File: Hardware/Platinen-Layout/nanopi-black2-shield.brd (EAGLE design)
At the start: 40 x 40 mm, 12 parts, among them IC2 LM3940IT-3.3

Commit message: new hardware + test code
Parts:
- added J3: (no value), 61300211821_Eagle_WR-PHD_rev19a:61300211121
- added R4, R5: 2.2k, SparkFun-Resistors:0603
- moved J5 0.42 mm to (38.4, 19.8), turned to 270 degrees
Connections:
- net 3.3V: now also R4.2, R5.2
- net 5V-1: now also J3.2
- net GND: now also J3.1
- net I2C_SCL0: now also R5.1
- net I2C_SDA0: now also R4.1
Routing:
- net 5V-1: track 31.1 -> 50.2 mm
- net 3.3V: track 15.3 -> 25.0 mm
- net GPIOA0: track 30.1 -> 24.4 mm
- net I2C_SCL0: track 34.9 -> 40.6 mm
- net I2C_SDA0: track 40.6 -> 36.4 mm
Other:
- outline, holes or cut-outs redrawn
- board text added: "5V_Ex"

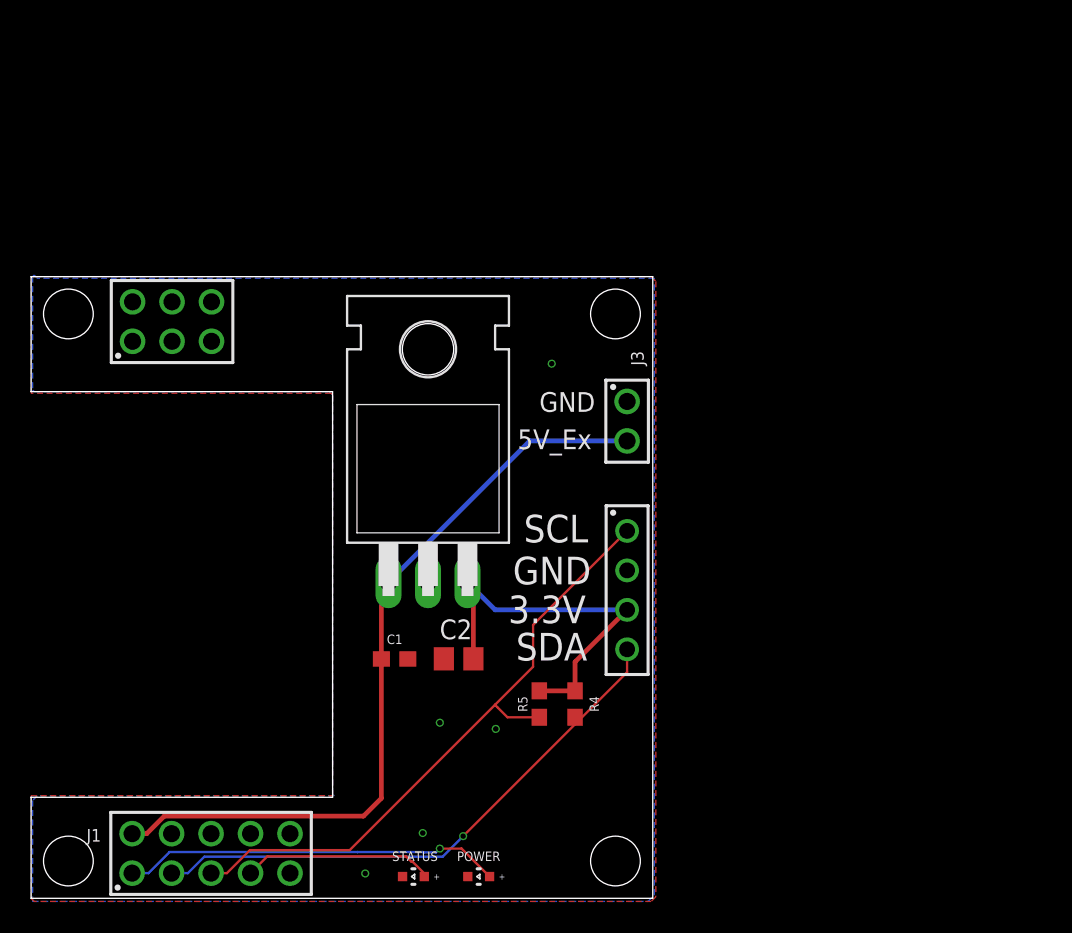
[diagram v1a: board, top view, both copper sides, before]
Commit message: new adapter Board
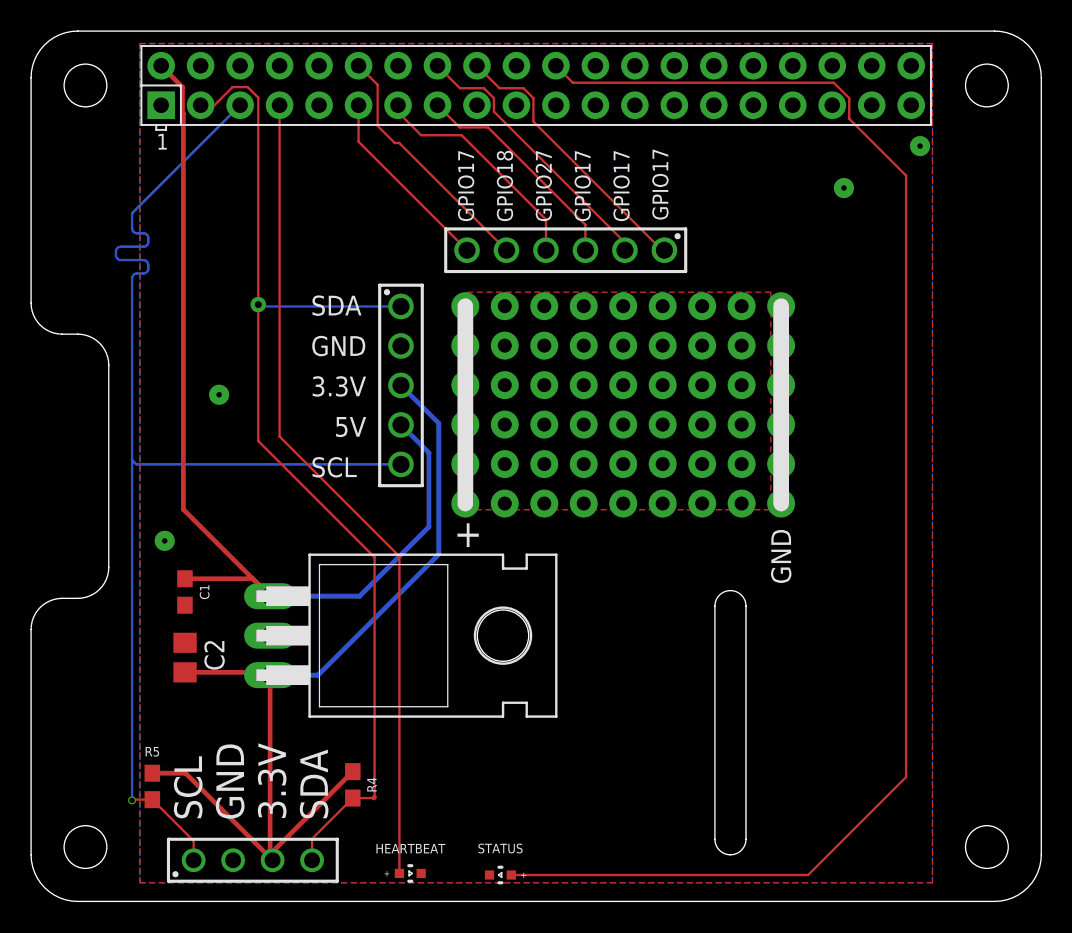
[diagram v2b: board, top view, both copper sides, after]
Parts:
- removed J3: (no value), 61300211821_Eagle_WR-PHD_rev19a:61300211121
- removed POWER: (no value), 155060GS75300_Eagle_WL-SMSW_rev20b:WL-SMSW_0603_REC
- removed U$1, U$2, U$3, U$4: (no value), M3-Hole:3-2MM-HOLE
- added HEARTBEAT: (no value), 155060GS75300_Eagle_WL-SMSW_rev20b:WL-SMSW_0603_REC
- added X1: RASPI_BOARD_B+#_HDC, raspberrypi_bastelstube_v13:RASPI_BOARD_B+HAT_DF_CF
- J1: device 61300211821_Eagle_WR-PHD_rev19a:61301021121 -> 61300621821_Eagle_WR-PHD_rev19a:61300511121
- J2: device 61300211821_Eagle_WR-PHD_rev19a:61300621121 -> 61300621821_Eagle_WR-PHD_rev19a:61300611121
- moved J1 32.5 mm to (23.8, 33.0), turned to 270 degrees
- moved J5 29.7 mm to (14.3, 2.45), turned to 0 degrees
- moved J2 25.7 mm to (34.4, 41.7), turned to 180 degrees
- moved R5 25.5 mm to (7.80, 7.20)
- moved C2 17.6 mm to (9.91, 15.5), turned to 90 degrees
- moved R4 15.2 mm to (20.7, 7.30)
- moved C1 14.2 mm to (9.90, 19.7), turned to 270 degrees
- moved IC2 13.6 mm to (25.5, 16.9), turned to 270 degrees
- moved STATUS 5.60 mm to (30.2, 1.50)
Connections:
- removed net 5V-2: J1.4
- removed net GPIOA0: J1.1, POWER.2
- removed net GPIOA2: J1.7, STATUS.2
- removed net UART1_RX: J1.10
- removed net UART1_TX: J1.8
- new net 3V3A: X1.1
- new net 3V3B: X1.17
- new net 5V0B: X1.4
- new net GND_A: X1.6
- new net GND_B: X1.9
- new net GND_C: X1.14
- new net GND_D: X1.20
- new net GND_E: X1.25
- new net GND_F: X1.30
- new net GND_G: X1.34
- new net GPIO04: HEARTBEAT.2, X1.7
- new net GPIO17: J2.6, X1.11
- new net GPIO18: J2.5, X1.12
- new net GPIO22: J2.3, X1.15
- new net GPIO23: J2.2, X1.16
- new net GPIO24: J2.1, X1.18
- new net GPIO25: STATUS.2, X1.22
- new net GPIO27: J2.4, X1.13
- net 3.3V: now also J1.3
- net 5V-1: now also J1.4, X1.2; no longer J1.2, J3.2
- net GND: now also HEARTBEAT.1, J1.2, X1.39; no longer J1.9, J3.1, POWER.1
- net I2C_SCL0: now also X1.5
- net I2C_SDA0: now also J1.1, X1.3; no longer J1.3
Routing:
- net GPIO25: track 0.00 -> 92.9 mm
- net GPIO04: track 0.00 -> 52.6 mm
- net 3.3V: track 25.0 -> 61.4 mm
- net I2C_SCL0: track 40.6 -> 76.1 mm, vias 0 -> 1
- net I2C_SDA0: track 36.4 -> 68.3 mm
- net GPIOA0: track 24.4 -> 0.00 mm, vias 1 -> 0
- net GPIO24: track 0.00 -> 17.9 mm
- net GPIO23: track 0.00 -> 17.8 mm
- net GPIO18: track 0.00 -> 16.0 mm
- net GPIO27: track 0.00 -> 14.8 mm
- net GPIO22: track 0.00 -> 14.3 mm
- net PLUS: track 0.00 -> 12.7 mm, vias 0 -> 6
- net GPIOA2: track 12.3 -> 0.00 mm
- net GPIO17: track 0.00 -> 12.2 mm
- net 5V-1: track 50.2 -> 62.4 mm
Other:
- board size 40 x 40 mm -> 65 x 56 mm
- board text added: "+"
- board text added: "5V"
- board text added: "GPIO17"
- board text added: "GPIO18"
- board text added: "GPIO27"
- board text removed: "5V_Ex"
